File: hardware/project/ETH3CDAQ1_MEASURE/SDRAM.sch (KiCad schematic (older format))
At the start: 8 parts, among them U501 IS42S16400J-xC

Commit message: PCB layout
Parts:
- U501: value IS42S16400J-xC -> IS42S16400J-xC/MT48LC16M16A2P-6A
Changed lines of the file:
@@
 P 5650 3200
 F 0 "U501" H 6400 4600 50  0000 C CNN
-F 1 "IS42S16400J-xC" H 6400 4500 50  0000 C CNN
+F 1 "IS42S16400J-xC/MT48LC16M16A2P-6A" H 6750 4500 50  0000 C CNN
 F 2 "ETH3CDAQ1:TSSOP-54" H 5650 3200 50  0001 C CNN
 F 3 "http://www.issi.com/WW/pdf/42-45S16400J.pdf" H 5050 4450 50  0001 C CNN

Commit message: PCB layout
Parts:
- renumbered C501 to C1401, C502 to C1402, C503 to C1403, C504 to C1404, C505 to C1405, C506 to C1406, C507 to C1407, U501 to U1401
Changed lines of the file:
@@
 $Descr A4 11693 8268
 encoding utf-8
-Sheet 5 15
+Sheet 14 15
 Title "SDRAM"
 Date "2020-03-07"
@@
 $EndDescr
 $Comp
-L Memory_RAM:IS42S16400J-xC U501
+L Memory_RAM:IS42S16400J-xC U1401
 U 1 1 5EB98CAA
 P 5650 3200
-F 0 "U501" H 6400 4600 50  0000 C CNN
+F 0 "U1401" H 6400 4600 50  0000 C CNN
 F 1 "IS42S16400J-xC/MT48LC16M16A2P-6A" H 6750 4500 50  0000 C CNN
 F 2 "ETH3CDAQ1:TSSOP-54" H 5650 3200 50  0001 C CNN
@@
 D[0..15]
 $Comp
-L Device:C C501
+L Device:C C1401
 U 1 1 5F12988C
 P 1000 7250
-F 0 "C501" H 1115 7296 50  0000 L CNN
+F 0 "C1401" H 1115 7296 50  0000 L CNN
 F 1 "100n" H 1115 7205 50  0000 L CNN
 F 2 "Capacitor_SMD:C_0603_1608Metric_Pad1.08x0.95mm_HandSolder" H 1038 7100 50  0001 C CNN
@@
 $EndComp
 $Comp
-L Device:C C502
+L Device:C C1402
 U 1 1 5F12BD5A
 P 1500 7250
-F 0 "C502" H 1615 7296 50  0000 L CNN
+F 0 "C1402" H 1615 7296 50  0000 L CNN
 F 1 "100n" H 1615 7205 50  0000 L CNN
 F 2 "Capacitor_SMD:C_0603_1608Metric_Pad1.08x0.95mm_HandSolder" H 1538 7100 50  0001 C CNN
@@
 $EndComp
 $Comp
-L Device:C C503
+L Device:C C1403
 U 1 1 5F12CAA5
 P 2000 7250
-F 0 "C503" H 2115 7296 50  0000 L CNN
+F 0 "C1403" H 2115 7296 50  0000 L CNN
 F 1 "100n" H 2115 7205 50  0000 L CNN
 F 2 "Capacitor_SMD:C_0603_1608Metric_Pad1.08x0.95mm_HandSolder" H 2038 7100 50  0001 C CNN
@@
 $EndComp
 $Comp
-L Device:C C504
+L Device:C C1404
 U 1 1 5F12CAAB
 P 2500 7250
-F 0 "C504" H 2615 7296 50  0000 L CNN
+F 0 "C1404" H 2615 7296 50  0000 L CNN
 F 1 "100n" H 2615 7205 50  0000 L CNN
 F 2 "Capacitor_SMD:C_0603_1608Metric_Pad1.08x0.95mm_HandSolder" H 2538 7100 50  0001 C CNN
@@
 $EndComp
 $Comp
-L Device:C C505
+L Device:C C1405
 U 1 1 5F12F1B4
 P 3000 7250
-F 0 "C505" H 3115 7296 50  0000 L CNN
+F 0 "C1405" H 3115 7296 50  0000 L CNN
 F 1 "100n" H 3115 7205 50  0000 L CNN
 F 2 "Capacitor_SMD:C_0603_1608Metric_Pad1.08x0.95mm_HandSolder" H 3038 7100 50  0001 C CNN
@@
 $EndComp
 $Comp
-L Device:C C506
+L Device:C C1406
 U 1 1 5F12F1BA
 P 3500 7250
-F 0 "C506" H 3615 7296 50  0000 L CNN
+F 0 "C1406" H 3615 7296 50  0000 L CNN
 F 1 "100n" H 3615 7205 50  0000 L CNN
 F 2 "Capacitor_SMD:C_0603_1608Metric_Pad1.08x0.95mm_HandSolder" H 3538 7100 50  0001 C CNN
@@
 $EndComp
 $Comp
-L Device:C C507
+L Device:C C1407
 U 1 1 5F12F1C0
 P 4000 7250
-F 0 "C507" H 4115 7296 50  0000 L CNN
+F 0 "C1407" H 4115 7296 50  0000 L CNN
 F 1 "100n" H 4115 7205 50  0000 L CNN
 F 2 "Capacitor_SMD:C_0603_1608Metric_Pad1.08x0.95mm_HandSolder" H 4038 7100 50  0001 C CNN
@@
 	2500 7000 2500 7050
 $Comp
-L power:GND #PWR0502
+L power:GND #PWR01402
 U 1 1 6038237F
 P 2500 7500
-F 0 "#PWR0502" H 2500 7250 50  0001 C CNN
+F 0 "#PWR01402" H 2500 7250 50  0001 C CNN
 F 1 "GND" H 2505 7327 50  0000 C CNN
 F 2 "" H 2500 7500 50  0001 C CNN
@@
 $EndComp
 $Comp
-L power:GND #PWR0504
+L power:GND #PWR01404
 U 1 1 603828AC
 P 5650 4700
-F 0 "#PWR0504" H 5650 4450 50  0001 C CNN
+F 0 "#PWR01404" H 5650 4450 50  0001 C CNN
 F 1 "GND" H 5655 4527 50  0000 C CNN
 F 2 "" H 5650 4700 50  0001 C CNN
@@
 $EndComp
 $Comp
-L power:+3.3V #PWR0503
+L power:+3.3V #PWR01403
 U 1 1 60383841
 P 5650 1700
-F 0 "#PWR0503" H 5650 1550 50  0001 C CNN
+F 0 "#PWR01403" H 5650 1550 50  0001 C CNN
 F 1 "+3.3V" H 5665 1873 50  0000 C CNN
 F 2 "" H 5650 1700 50  0001 C CNN
@@
 $EndComp
 $Comp
-L power:+3.3V #PWR0501
+L power:+3.3V #PWR01401
 U 1 1 60384354
 P 2500 7000
-F 0 "#PWR0501" H 2500 6850 50  0001 C CNN
+F 0 "#PWR01401" H 2500 6850 50  0001 C CNN
 F 1 "+3.3V" H 2515 7173 50  0000 C CNN
 F 2 "" H 2500 7000 50  0001 C CNN

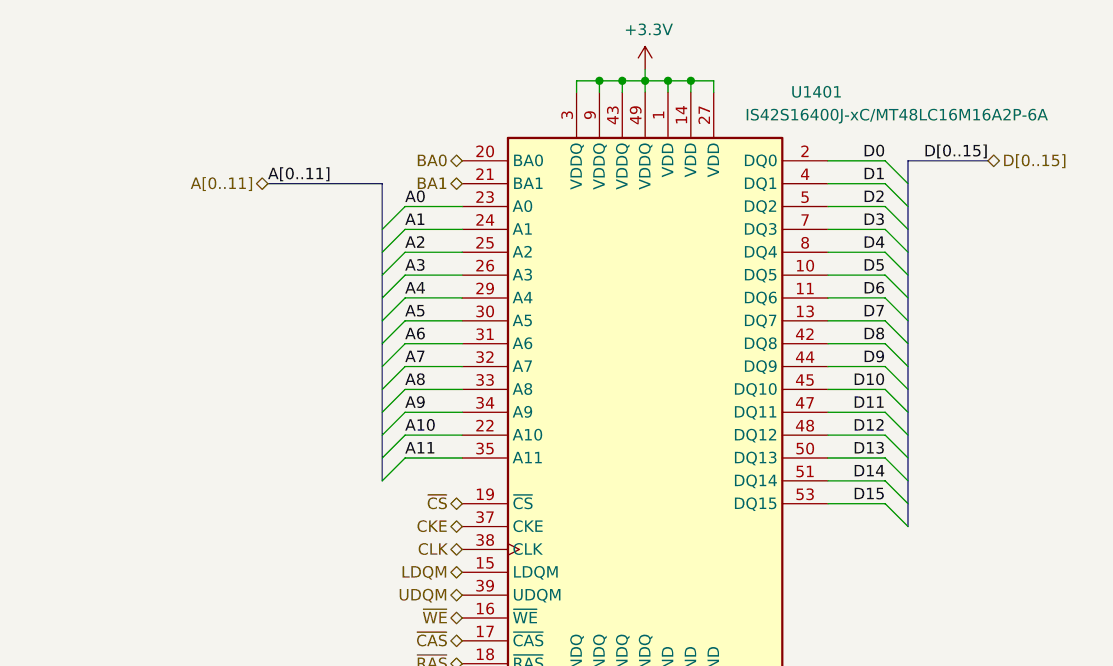
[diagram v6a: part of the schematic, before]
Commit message: Modification in PCBs. Created BOM files.
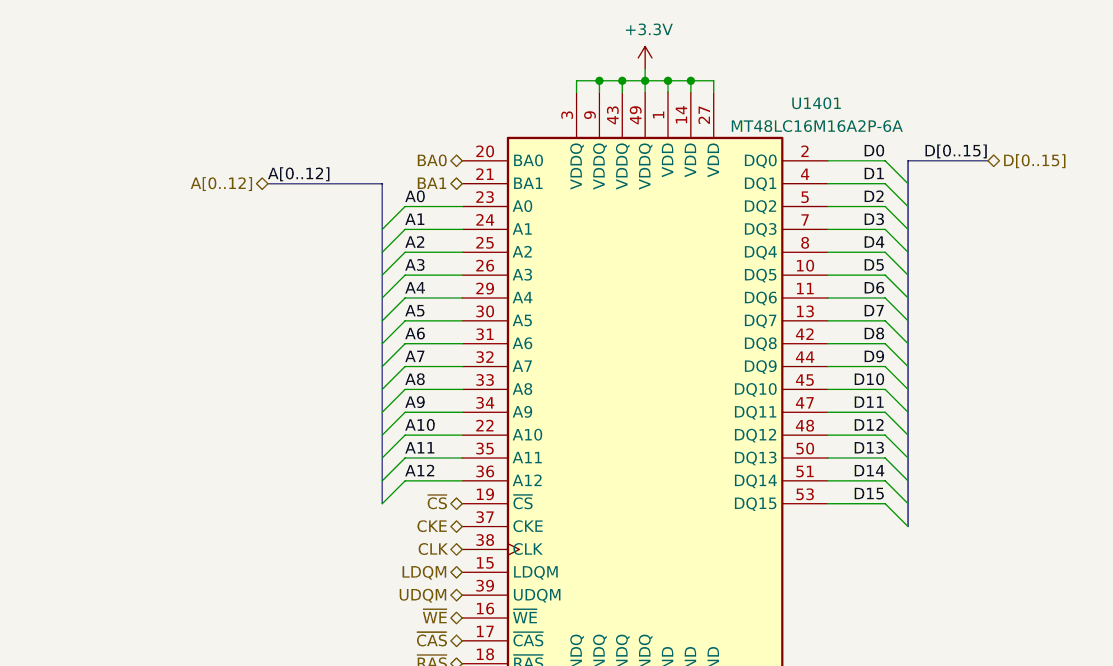
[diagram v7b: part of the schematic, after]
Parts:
- removed U1401: IS42S16400J-xC/MT48LC16M16A2P-6A, ETH3CDAQ1:TSSOP-54, symbol Memory_RAM:IS42S16400J-xC
- added U1401: MT48LC16M16A2P-6A, ETH3CDAQ1:TSSOP-54, symbol ETH3CDAQ1:MT48LC16M16A2P-6A
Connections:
- net +3V3: now also U1401.1 (VDD), U1401.14 (VDD), U1401.27 (VDD), U1401.3 (VDDQ), U1401.43 (VDDQ), U1401.49 (VDDQ), U1401.9 (VDDQ)
- net A0: now also U1401.23 (A0)
- net A1: now also U1401.24 (A1)
- net A10: now also U1401.22 (A10)
- net A11: now also U1401.35 (A11)
- net A2: now also U1401.25 (A2)
- net A3: now also U1401.26 (A3)
- net A4: now also U1401.29 (A4)
- net A5: now also U1401.30 (A5)
- net A6: now also U1401.31 (A6)
- net A7: now also U1401.32 (A7)
- net A8: now also U1401.33 (A8)
- net A9: now also U1401.34 (A9)
- net BA0: now also U1401.20 (BA0)
- net BA1: now also U1401.21 (BA1)
- net CKE: now also U1401.37 (CKE)
- net CLK: now also U1401.38 (CLK)
- net D0: now also U1401.2 (DQ0)
- net D1: now also U1401.4 (DQ1)
- net D10: now also U1401.45 (DQ10)
- net D11: now also U1401.47 (DQ11)
- net D12: now also U1401.48 (DQ12)
- net D13: now also U1401.50 (DQ13)
- net D14: now also U1401.51 (DQ14)
- net D15: now also U1401.53 (DQ15)
- net D2: now also U1401.5 (DQ2)
- net D3: now also U1401.7 (DQ3)
- net D4: now also U1401.8 (DQ4)
- net D5: now also U1401.10 (DQ5)
- net D6: now also U1401.11 (DQ6)
- net D7: now also U1401.13 (DQ7)
- net D8: now also U1401.42 (DQ8)
- net D9: now also U1401.44 (DQ9)
- net GND: now also U1401.12 (GNDQ), U1401.28 (GND), U1401.41 (GND), U1401.46 (GNDQ), U1401.52 (GNDQ), U1401.54 (GND), U1401.6 (GNDQ)
- net LDQM: now also U1401.15 (LDQM)
- net UDQM: now also U1401.39 (UDQM)
- net ~CAS: now also U1401.17 (~CAS)
- net ~CS: now also U1401.19 (~CS)
- net ~RAS: now also U1401.18 (~RAS)
- net ~WE: now also U1401.16 (~WE)
- new net A12: U1401.36 (A12)
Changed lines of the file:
@@
 Comment4 ""
 $EndDescr
-$Comp
-L Memory_RAM:IS42S16400J-xC U1401
-U 1 1 5EB98CAA
-P 5650 3200
-F 0 "U1401" H 6400 4600 50  0000 C CNN
-F 1 "IS42S16400J-xC/MT48LC16M16A2P-6A" H 6750 4500 50  0000 C CNN
-F 2 "ETH3CDAQ1:TSSOP-54" H 5650 3200 50  0001 C CNN
-F 3 "http://www.issi.com/WW/pdf/42-45S16400J.pdf" H 5050 4450 50  0001 C CNN
-	1    5650 3200
-	1    0    0    -1
-$EndComp
 Wire Wire Line
 	5350 4600 5350 4650
@@
 D[0..15]
 Text Label 4000 2200 0    50   ~ 0
-A[0..11]
+A[0..12]
 Text HLabel 4000 2200 0    50   BiDi ~ 0
-A[0..11]
+A[0..12]
 Text HLabel 7150 2100 2    50   BiDi ~ 0
 D[0..15]
@@
 	1    0    0    -1
 $EndComp
+$Comp
+L ETH3CDAQ1:MT48LC16M16A2P-6A U1401
+U 1 1 5FD364EC
+P 5650 3200
+F 0 "U1401" H 6400 4550 50  0000 C CNN
+F 1 "MT48LC16M16A2P-6A" H 6400 4450 50  0000 C CNN
+F 2 "ETH3CDAQ1:TSSOP-54" H 5650 3200 50  0001 C CNN
+F 3 "" H 5050 4450 50  0001 C CNN
+	1    5650 3200
+	1    0    0    -1
+$EndComp
+Wire Wire Line
+	4850 3500 4600 3500
+Text Label 4600 3500 0    50   ~ 0
+A12
+Entry Wire Line
+	4600 3500 4500 3600
 Wire Bus Line
-	4500 2200 4500 3500
+	4500 2200 4500 3600
 Wire Bus Line
 	6800 2100 6800 3700
